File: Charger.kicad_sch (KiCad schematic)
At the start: 63 parts, among them Q6 BSC0702LS, Q7 BSC0702LS, Q8 BSC0702LS, Q9 BSC0702LS, U27 BQ25756RRVR

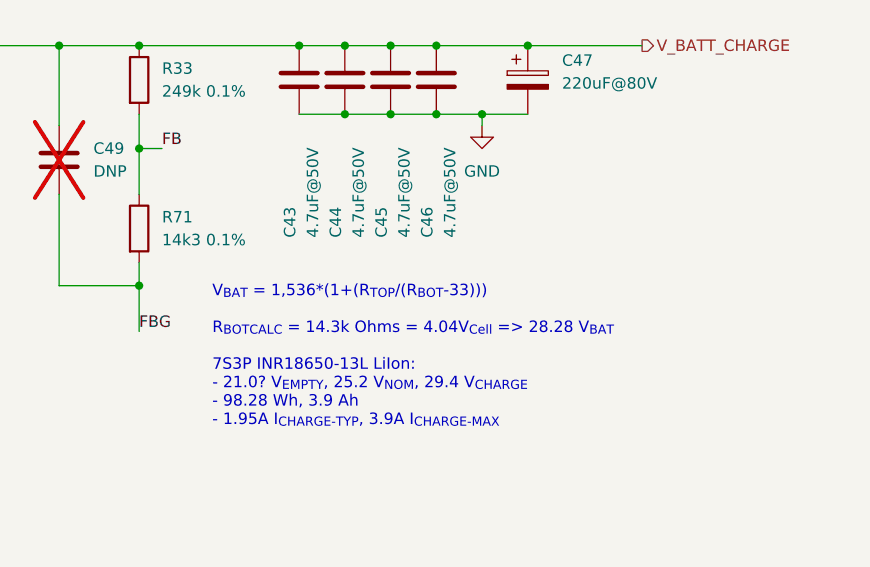
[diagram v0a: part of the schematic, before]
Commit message: - Increase charger Vfb
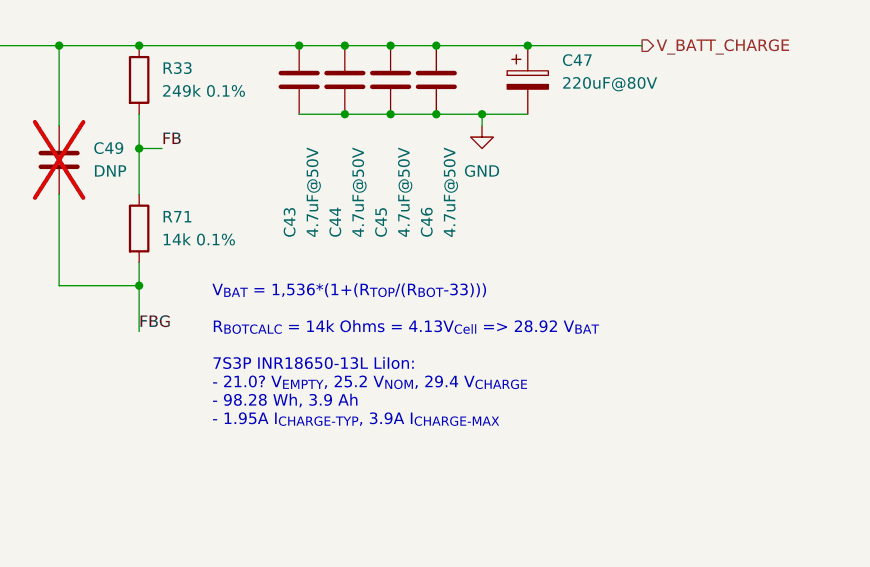
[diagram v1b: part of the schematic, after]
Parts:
- R71: value 14k3 0.1% -> 14k 0.1%; LCSC Part # C861131 -> C2924128; PN RT0603BRD0714K3L -> AR03BTCX1402A
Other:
- note added: "V_{BAT} = 1,536*(1+(R_{TOP}/(R_{BOT}-33))) R_{BOTCALC} = 14k Ohms = 4.13V_{Cell} => 28.92 V_{BAT} 7S3P INR18650-13L LiIon: - 21.0? V_{EMPTY}, 25.2 V_{NOM}, 29.4 V_{CHARGE} - 98.28 Wh, 3.9 Ah - 1.95A I_{CHARGE-TYP}, 3.9A I_{CHARGE-MAX}"
- note removed: "V_{BAT} = 1,536*(1+(R_{TOP}/(R_{BOT}-33))) R_{BOTCALC} = 14.3k Ohms = 4.04V_{Cell} => 28.28 V_{BAT} 7S3P INR18650-13L LiIon: - 21.0? V_{EMPTY}, 25.2 V_{NOM}, 29.4 V_{CHARGE} - 98.28 Wh, 3.9 Ah - 1.95A I_{CHARGE-TYP}, 3.9A I_{CHARGE-MAX}"
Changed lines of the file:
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@@
 		)
 	)
-	(text "V_{BAT} = 1,536*(1+(R_{TOP}/(R_{BOT}-33)))\n\nR_{BOTCALC} = 14.3k Ohms = 4.04V_{Cell} => 28.28 V_{BAT}\n\n7S3P INR18650-13L LiIon:\n- 21.0? V_{EMPTY}, 25.2 V_{NOM}, 29.4 V_{CHARGE}\n- 98.28 Wh, 3.9 Ah\n- 1.95A I_{CHARGE-TYP}, 3.9A I_{CHARGE-MAX}"
+	(text "V_{BAT} = 1,536*(1+(R_{TOP}/(R_{BOT}-33)))\n\nR_{BOTCALC} = 14k Ohms = 4.13V_{Cell} => 28.92 V_{BAT}\n\n7S3P INR18650-13L LiIon:\n- 21.0? V_{EMPTY}, 25.2 V_{NOM}, 29.4 V_{CHARGE}\n- 98.28 Wh, 3.9 Ah\n- 1.95A I_{CHARGE-TYP}, 3.9A I_{CHARGE-MAX}"
 		(exclude_from_sim no)
 		(at 342.138 166.624 0)
@@
 			)
 		)
-		(property "Value" "14k3 0.1%"
+		(property "Value" "14k 0.1%"
 			(at 336.55 153.6699 0)
 			(show_name no)
@@
 			)
 		)
-		(property "Description" "-55℃~+155℃ 100mW 14.3kΩ 75V Thin Film Resistor ±0.1% ±25ppm/℃ 0603 Chip Resistor - Surface Mount ROHS"
+		(property "Description" "-55℃~+155℃ 100mW 14kΩ 75V Thin Film Resistor ±0.1% ±25ppm/℃ 0603 Chip Resistor - Surface Mount ROHS"
 			(at 334.01 152.4 0)
 			(hide yes)
@@
 			)
 		)
-		(property "PN" "RT0603BRD0714K3L"
+		(property "PN" "AR03BTCX1402A"
 			(at 334.01 152.4 0)
 			(hide yes)
@@
 			)
 		)
-		(property "LCSC Part #" "C861131"
+		(property "LCSC Part #" "C2924128"
 			(at 334.01 152.4 0)
 			(hide yes)

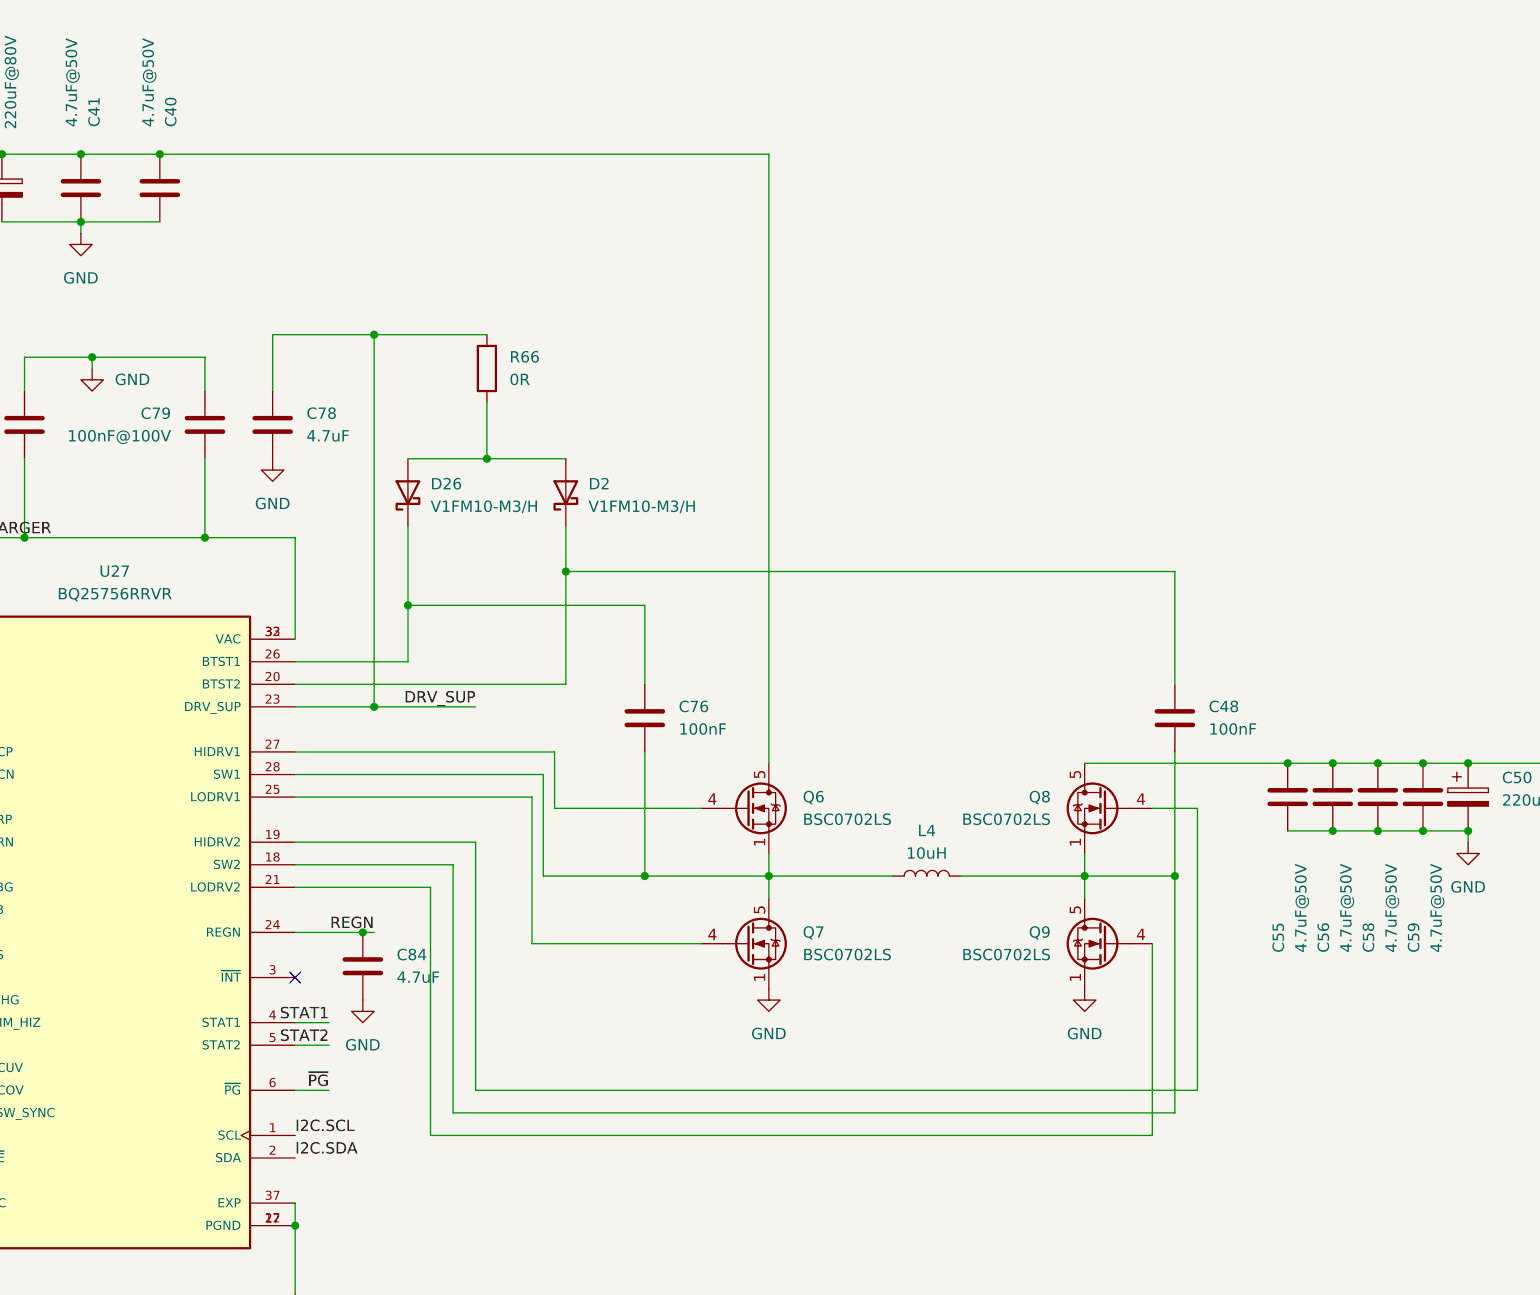
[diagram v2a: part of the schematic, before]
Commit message: Change charger FETs to AON7246E
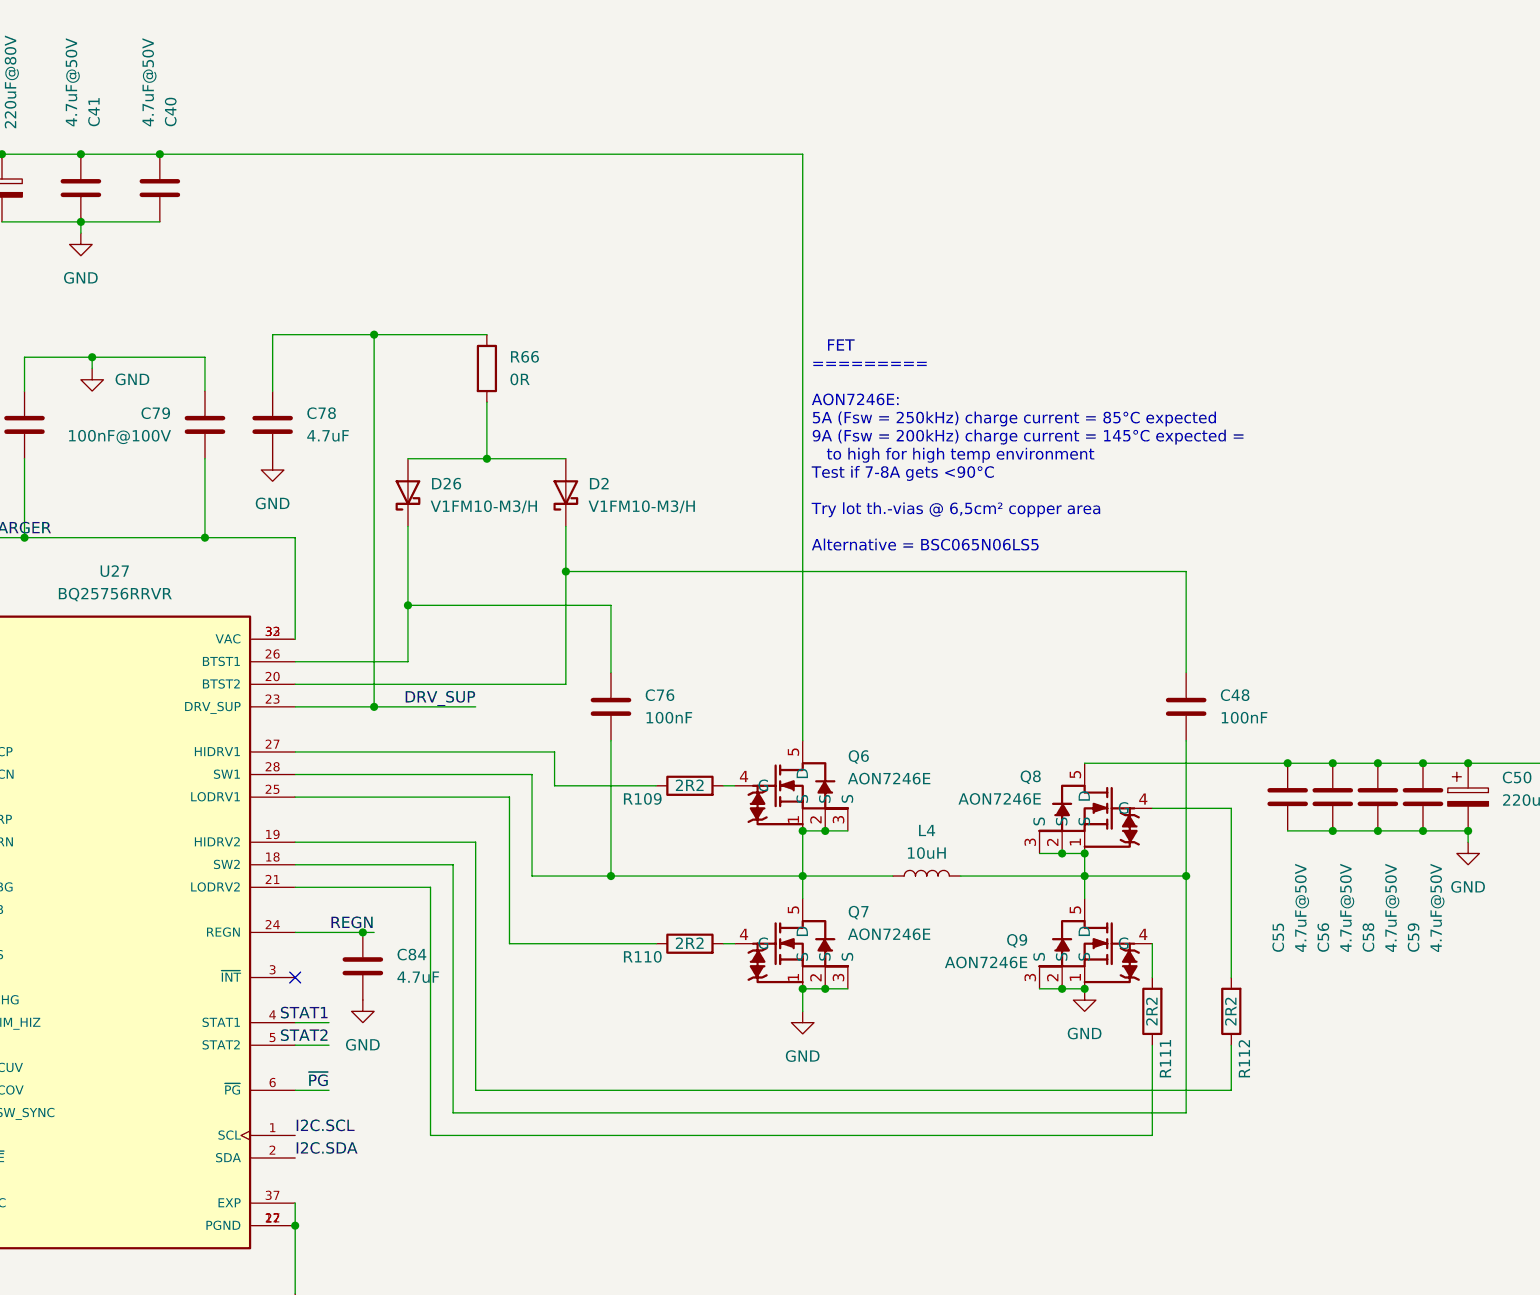
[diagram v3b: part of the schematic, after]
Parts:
- removed Q7, Q8, Q9: BSC0702LS, Package_TO_SOT_SMD:TDSON-8-1, symbol Transistor_FET:BSC070N10NS3G
- added Q7, Q8, Q9: AON7246E, nlbn:AON7246E_C3277811, symbol nlbn:AON7246E_C3277811
- added R109, R110, R111, R112: 2R2, Resistor_SMD:R_0603_1608Metric_Pad0.98x0.95mm_HandSolder, symbol Device:R
- Q6: value BSC0702LS -> AON7246E; footprint Package_TO_SOT_SMD:TDSON-8-1 -> nlbn:AON7246E_C3277811; symbol Transistor_FET:BSC070N10NS3G -> nlbn:AON7246E_C3277811; LCSC Part # C501503 -> C3277811
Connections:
- net GND: now also Q7.1 (S), Q7.2 (S), Q7.3 (S), Q9.1 (S), Q9.2 (S), Q9.3 (S)
- net at C48.2, L4.2, U27.18 (SW2): now also Q8.1 (S), Q8.2 (S), Q8.3 (S), Q9.5 (D)
- net at U27.19 (HIDRV2): now also R112.1
- net at U27.21 (LODRV2): now also R111.1
- net at U27.25 (LODRV1): now also R110.1
- net at U27.27 (HIDRV1): now also R109.1; no longer Q6.4 (G)
- net at C76.1, L4.1, Q6.1 (S)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: now also Q7.5 (D)
- net at C50.1, C55.1, C56.1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: now also Q8.5 (D)
- new net: Q8.4 (G), R112.2
- new net: Q6.4 (G), R109.2
- new net: Q7.4 (G), R110.2
- new net: Q9.4 (G), R111.2
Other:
- note added: "FET ========= AON7246E: 5A (Fsw = 250kHz) charge current = 85°C expected 9A (Fsw = 200kHz) charge current = 145°C expected = to high for high temp environment Test if 7-8A gets <90°C Try lot th.-vias @ 6,5cm² copper area Alternative = BSC065N06LS5"
- moved on the sheet: C48, C76

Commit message: Production preparation
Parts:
- C22, C38, C39, C40, C41, C43, C44, C45, C46, C55, C56, C58, C59: LCSC Part # C29823 -> C51205
- R109, R110, R111, R112: LCSC Part # LCSC Part -> C22939
